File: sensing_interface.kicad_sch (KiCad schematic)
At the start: 12 parts, among them U2 BMI270, U3 BMP388, U4 ASM330LHBTR

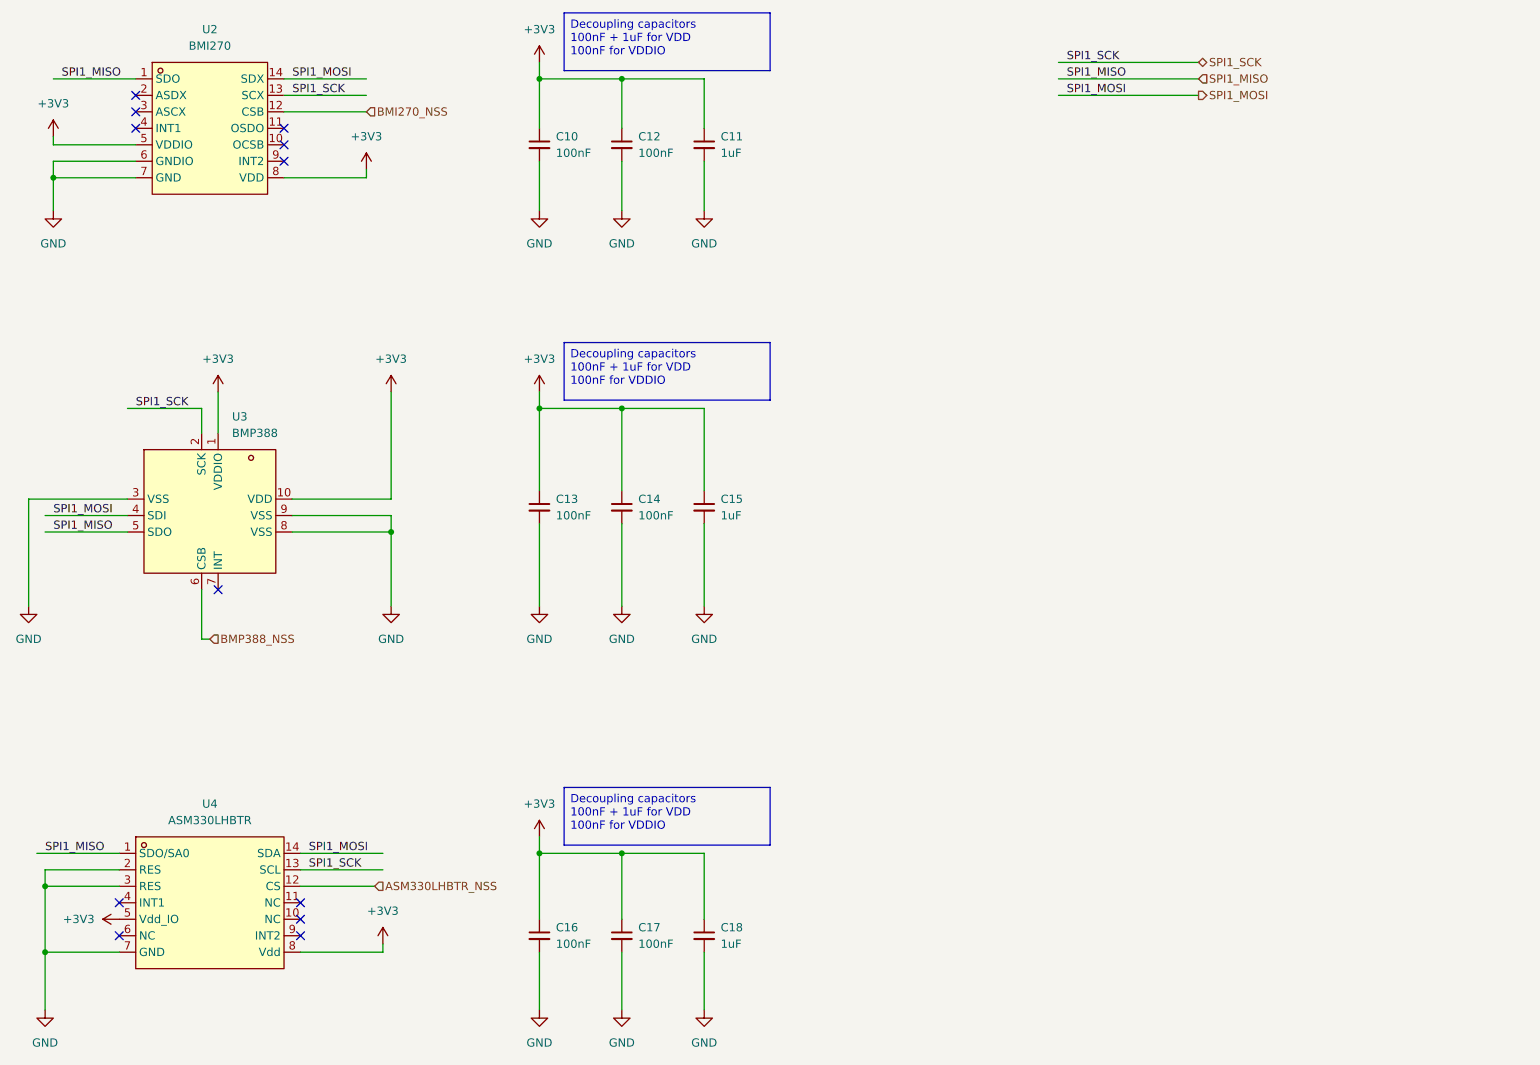
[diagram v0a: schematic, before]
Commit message: corrections and IO updated
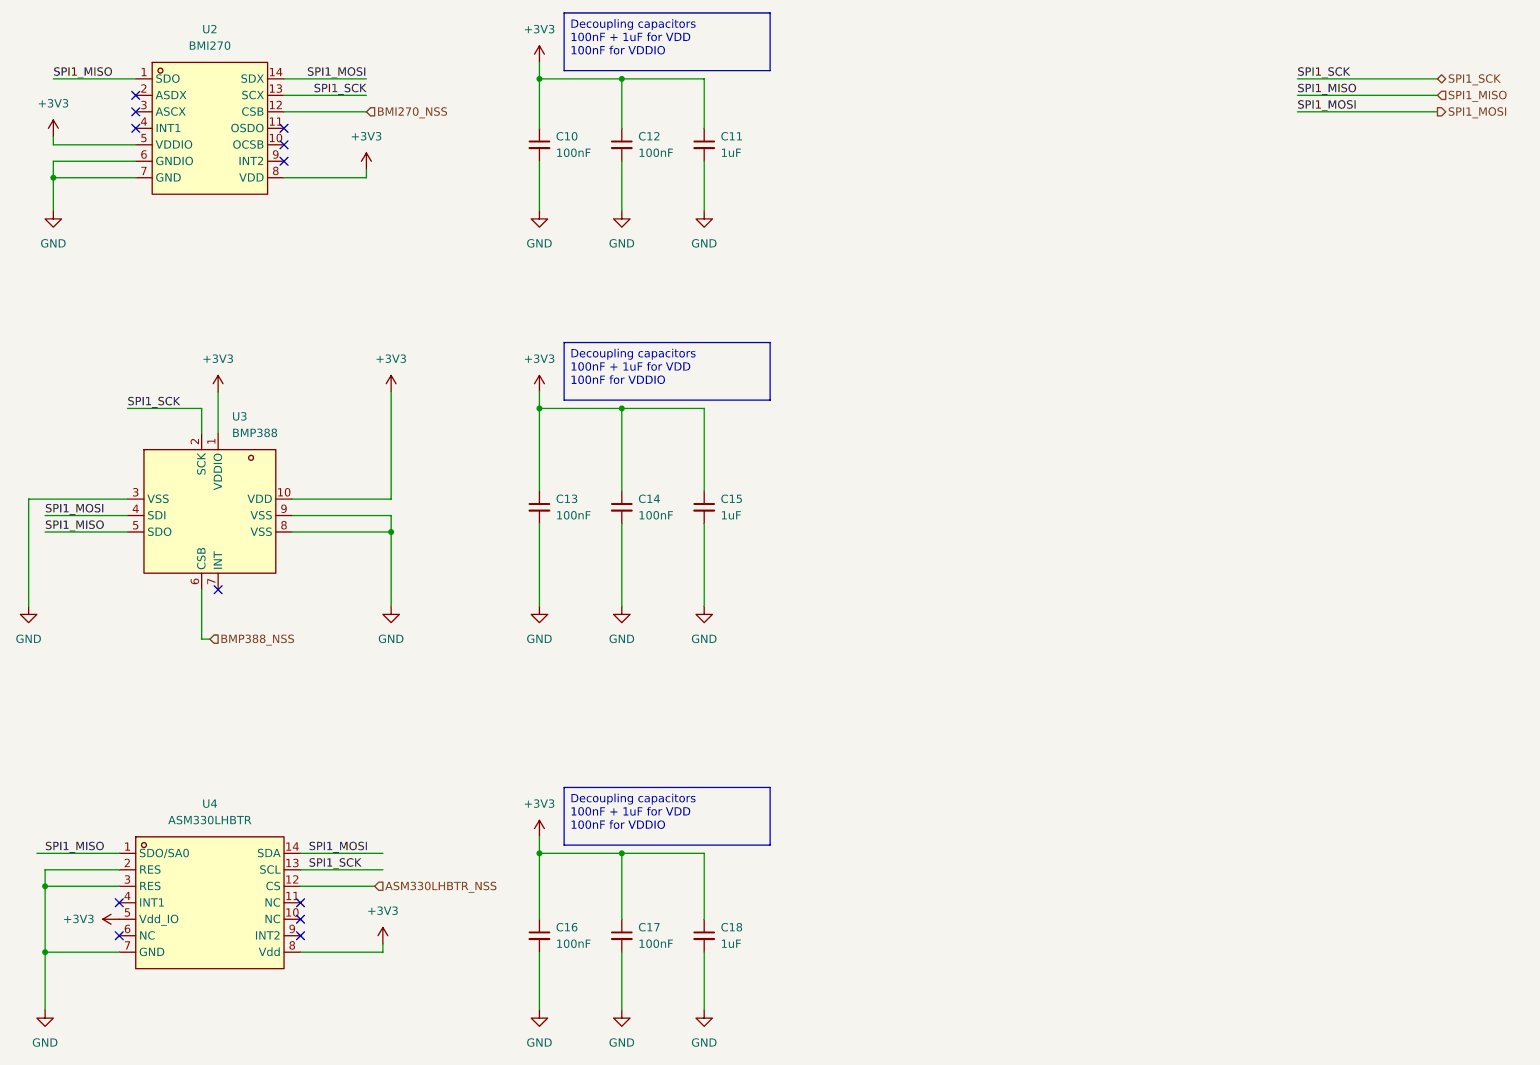
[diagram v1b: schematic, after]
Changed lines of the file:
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@@
-	(wire
-		(pts
-			(xy 194.31 25.4) (xy 215.9 25.4)
-		)
-		(stroke
-			(width 0)
-			(type default)
-		)
-	)
 	(wire
 		(pts
@@
 	(wire
 		(pts
+			(xy 38.1 97.79) (xy 50.8 97.79)
+		)
+		(stroke
+			(width 0)
+			(type default)
+		)
+	)
+	(wire
+		(pts
 			(xy 38.1 149.86) (xy 38.1 152.4)
 		)
@@
 	(wire
 		(pts
-			(xy 194.31 27.94) (xy 215.9 27.94)
+			(xy 231.14 30.48) (xy 252.73 30.48)
 		)
 		(stroke
@@
 	(wire
 		(pts
-			(xy 38.1 97.79) (xy 50.8 97.79)
-		)
-		(stroke
-			(width 0)
-			(type default)
-		)
-	)
-	(wire
-		(pts
 			(xy 76.2 97.79) (xy 91.44 97.79)
 		)
@@
 	(wire
 		(pts
+			(xy 39.37 27.94) (xy 52.07 27.94)
+		)
+		(stroke
+			(width 0)
+			(type default)
+		)
+	)
+	(wire
+		(pts
 			(xy 139.7 96.52) (xy 139.7 109.22)
 		)
@@
 	(wire
 		(pts
-			(xy 39.37 27.94) (xy 52.07 27.94)
-		)
-		(stroke
-			(width 0)
-			(type default)
-		)
-	)
-	(wire
-		(pts
 			(xy 127 27.94) (xy 114.3 27.94)
 		)
@@
 	(wire
 		(pts
+			(xy 231.14 27.94) (xy 252.73 27.94)
+		)
+		(stroke
+			(width 0)
+			(type default)
+		)
+	)
+	(wire
+		(pts
 			(xy 127 96.52) (xy 127 109.22)
 		)
@@
 	(wire
 		(pts
-			(xy 194.31 30.48) (xy 215.9 30.48)
+			(xy 231.14 33.02) (xy 252.73 33.02)
 		)
 		(stroke
@@
 	)
 	(label "SPI1_MOSI"
-		(at 39.37 95.25 0)
+		(at 38.1 95.25 0)
 		(effects
 			(font
@@
 	)
 	(label "SPI1_MOSI"
-		(at 195.58 30.48 0)
+		(at 231.14 33.02 0)
 		(effects
 			(font
@@
 	)
 	(label "SPI1_SCK"
-		(at 52.07 78.74 0)
+		(at 50.8 78.74 0)
 		(effects
 			(font
@@
 	)
 	(label "SPI1_MISO"
-		(at 195.58 27.94 0)
+		(at 231.14 30.48 0)
 		(effects
 			(font
@@
 	)
 	(label "SPI1_MISO"
-		(at 40.64 27.94 0)
+		(at 39.37 27.94 0)
 		(effects
 			(font
@@
 	)
 	(label "SPI1_MOSI"
-		(at 76.2 27.94 0)
-		(effects
-			(font
-				(size 1.27 1.27)
-			)
-			(justify left bottom)
+		(at 87.63 27.94 180)
+		(effects
+			(font
+				(size 1.27 1.27)
+			)
+			(justify right bottom)
 		)
 	)
 	(label "SPI1_MISO"
-		(at 39.37 97.79 0)
+		(at 38.1 97.79 0)
 		(effects
 			(font
@@
 	)
 	(label "SPI1_SCK"
-		(at 195.58 25.4 0)
+		(at 231.14 27.94 0)
 		(effects
 			(font
@@
 	)
 	(label "SPI1_SCK"
-		(at 76.2 30.48 0)
-		(effects
-			(font
-				(size 1.27 1.27)
-			)
-			(justify left bottom)
+		(at 87.63 30.48 180)
+		(effects
+			(font
+				(size 1.27 1.27)
+			)
+			(justify right bottom)
 		)
 	)
 	(hierarchical_label "SPI1_MOSI"
 		(shape output)
-		(at 215.9 30.48 0)
+		(at 252.73 33.02 0)
 		(effects
 			(font
@@
 	(hierarchical_label "SPI1_MISO"
 		(shape input)
-		(at 215.9 27.94 0)
+		(at 252.73 30.48 0)
 		(effects
 			(font
@@
 	(hierarchical_label "SPI1_SCK"
 		(shape bidirectional)
-		(at 215.9 25.4 0)
-		(effects
-			(font
+		(at 252.73 27.94 0)
+		(effects
+			(font

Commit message: finalized RF
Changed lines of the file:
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@@
 	(wire
 		(pts
-			(xy 231.14 30.48) (xy 252.73 30.48)
+			(xy 196.85 36.83) (xy 218.44 36.83)
 		)
 		(stroke
@@
 	(wire
 		(pts
-			(xy 231.14 27.94) (xy 252.73 27.94)
+			(xy 196.85 34.29) (xy 218.44 34.29)
 		)
 		(stroke
@@
 	(wire
 		(pts
-			(xy 231.14 33.02) (xy 252.73 33.02)
+			(xy 196.85 39.37) (xy 218.44 39.37)
 		)
 		(stroke
@@
 	)
 	(label "SPI1_MOSI"
-		(at 231.14 33.02 0)
+		(at 196.85 39.37 0)
 		(effects
 			(font
@@
 	)
 	(label "SPI1_MISO"
-		(at 231.14 30.48 0)
+		(at 196.85 36.83 0)
 		(effects
 			(font
@@
 	)
 	(label "SPI1_SCK"
-		(at 231.14 27.94 0)
+		(at 196.85 34.29 0)
 		(effects
 			(font
@@
 	(hierarchical_label "SPI1_MOSI"
 		(shape output)
-		(at 252.73 33.02 0)
+		(at 218.44 39.37 0)
 		(effects
 			(font
@@
 	(hierarchical_label "SPI1_MISO"
 		(shape input)
-		(at 252.73 30.48 0)
+		(at 218.44 36.83 0)
 		(effects
 			(font
@@
 	(hierarchical_label "SPI1_SCK"
 		(shape bidirectional)
-		(at 252.73 27.94 0)
-		(effects
-			(font
+		(at 218.44 34.29 0)
+		(effects
+			(font
